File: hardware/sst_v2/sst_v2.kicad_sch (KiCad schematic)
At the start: 92 parts, among them U1 Pico_2_W, U2 ADS131M04IPWR, U3 DS3231SN, Y1 ECS-2520MVLC-081.92-BN-TR

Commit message: hw: Rev. 3 Review — LDO-Pinbelegung, VSYS-Diode, Verpolschutz, Fertigungsdaten
Fehler behoben:
- TPS7A4700: Symbol nach SBVS204G (GND-Pin lag an 3,3 V, OUT/IN vertauscht,
  ANY-OUT an 3,3 V), Footprint Texas RGW0020A, LDO-Bereich neu geroutet,
  Eingangs-C 10 uF (C22), Ausgangs-C 22 uF (C6)
- USB-VBUS speiste in den LiPo: Schottky D_VSYS1 zwischen +VBAT_SW und VSYS
- RTC-Backup-Diode verpolt: entfernt, CR1220 direkt an VBAT
- Buzzer-Footprint auf 5-mm-Raster (TDK PS1240P02BT)
- R18 an 3V3_EN entfernt, DS3231-RST offen
- ADS131M04 DVDD aus +3V3_DIG über FB1 (Logikpegel 3,3 V)
- CMC nach Murata-Ersatzschaltbild beschaltet (Gleichtaktdämpfung)
- J_DEBUG1 als 1x3 UART (SWD-Pins waren unverbunden)
- DRC: Lötstopp-Steg 0,1 mm, Kupfer-Kante 0,3 mm, J_SD1-Schirm-Pads gekürzt,
  volle Anbindung der GND-Pads

Empfehlungen umgesetzt: Verpolschutz Q_RP1 (DMG2305UX), Polymer-Tantal C26,
1 uF direkt an AVDD, 100 nF an 74HC4040 (C44), microSD-DAT1-Pull-up (R48),
Montagelöcher im Schaltplan, Silkscreen bereinigt.

ERC 0 Fehler, DRC 0 Fehler/0 offene Verbindungen/0 Paritätsfehler.
Gerber, Bohrdaten, BOM und CPL neu erzeugt. README für Rev. 3 neu.

Co-Authored-By: Claude Opus 5.5 <noreply@anthropic.com>
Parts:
- removed D_RTC1: 1N4148, Diode_SMD:D_SOD-123, symbol sst_v2_local:Diode
- removed R18: 10k, Resistor_SMD:R_0603_1608Metric, symbol sst_v2_local:R
- added C44: 100nF X7R, Capacitor_SMD:C_0603_1608Metric, symbol sst_v2_local:C
- added D_VSYS1: PMEG3020EH, Diode_SMD:D_SOD-123F, symbol sst_v2_local:Diode
- added H1, H2, H3, H4: M3_NPTH, MountingHole:MountingHole_3.2mm_M3, symbol sst_v2_local:MountingHole
- added Q_RP1: DMG2305UX, Package_TO_SOT_SMD:SOT-23, symbol sst_v2_local:DMG2305UX
- added R47: 10k, Resistor_SMD:R_0603_1608Metric, symbol sst_v2_local:R
- added R48: 47k, Resistor_SMD:R_0603_1608Metric, symbol sst_v2_local:R
- BZ1: footprint Buzzer_Beeper:Buzzer_12x9.5RM7.6 -> Buzzer_Beeper:Buzzer_TDK_PS1240P02BT_D12.2mm_H6.5mm
- C1: value 1uF X7R -> 100nF X7R
- C22: value 10uF X7R -> 10uF X5R; footprint Capacitor_SMD:C_0805_2012Metric -> Capacitor_SMD:C_0603_1608Metric
- C23: value 100nF X7R -> 1uF X7R
- C26: value 100uF/10V Tant -> 100uF 10V Polymer
- C6: value 10uF X7R -> 22uF X7R
- J_DEBUG1: value SWD+UART Header 1x5 -> UART Header 1x3; footprint Connector_PinHeader_2.54mm:PinHeader_1x05_P2.54mm_Vertical -> Connector_PinHeader_2.54mm:PinHeader_1x03_P2.54mm_Vertical; symbol sst_v2_local:Conn_5P -> sst_v2_local:Conn_1x03
- U_ANA_LDO1: footprint Package_DFN_QFN:QFN-20-1EP_5x5mm_P0.65mm_EP3.35x3.35mm -> Package_DFN_QFN:Texas_RGW0020A_VQFN-20-1EP_5x5mm_P0.65mm_EP3.15x3.15mm
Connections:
- net +3V0_ANA_FB is gone; now on net +3V3_DIG: U_ANA_LDO1.13 (EN), U_ANA_LDO1.15 (IN)
- net RTC_BAT_RAW is gone; now on net RTC_VBAT: BT1.1 (+)
- net SWCLK is gone; now on net GND: J_DEBUG1.3
- net +3V0_ANA: now also U_ANA_LDO1.1 (OUT), U_ANA_LDO1.20 (OUT), U_ANA_LDO1.3 (SENSE); no longer C22.1, FB1.1, U_ANA_LDO1.16 (OUT), U_ANA_LDO1.17 (OUT), U_ANA_LDO1.18 (OUT)
- net +3V3_DIG: now also C22.1, FB1.1, U_ANA_LDO1.16 (IN), C44.1, R48.2; no longer U3.4 (RST), U_ANA_LDO1.1 (IN), U_ANA_LDO1.12 (ANY7), U_ANA_LDO1.2 (IN), U_ANA_LDO1.3 (EN), U_ANA_LDO1.7 (ANY2), U_ANA_LDO1.8 (ANY3)
- net +VBAT: now also Q_RP1.2 (S); no longer J_BAT1.1
- net +VBAT_SW: now also D_VSYS1.2 (A); no longer U1.39 (VSYS)
- net FORK_POT_GND_F: now also L_FORK_CMC1.1; no longer L_FORK_CMC1.2
- net GND: now also U_ANA_LDO1.7 (GND), U_ANA_LDO1.8 (1P6V), C44.2, R47.2; no longer J_DEBUG1.5, U_ANA_LDO1.10 (ANY5), U_ANA_LDO1.11 (ANY6), U_ANA_LDO1.14 (GND), U_ANA_LDO1.5 (GND), U_ANA_LDO1.6 (ANY1), U_ANA_LDO1.9 (ANY4)
- net J_FORK_POT_GND: now also L_FORK_CMC1.2; no longer L_FORK_CMC1.1
- net J_SHOCK_POT_GND: now also L_SHOCK_CMC1.2; no longer L_SHOCK_CMC1.1
- net LDO_NRSS: now also U_ANA_LDO1.14 (NR); no longer U_ANA_LDO1.4 (NR/SS)
- net SHOCK_POT_GND_F: now also L_SHOCK_CMC1.1; no longer L_SHOCK_CMC1.2
- net +3V3_EN: no longer names the net of U1.37 (3V3_EN)
- net SD_NC2 renamed SD_DAT1
- net SD_DAT1: now also R48.1
- removed net SWDIO: J_DEBUG1.4
- new net Q_RP_G: Q_RP1.1 (G), R47.1
- new net VBAT_IN: J_BAT1.1, Q_RP1.3 (D)
- new net VSYS: D_VSYS1.1 (K), U1.39 (VSYS)
- no-connect marks 25 -> 31
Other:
- note added: "POWER — LiPo → SW → Schottky → VSYS +VBAT_SW → D_VSYS1 (PMEG3020EH) → VSYS (Pico) TPS7A4700: +3V3_DIG → +3V0_ANA"
- note added: "STORAGE / RTC / DISPLAY MicroSD J_SD on spi0 (GP16-19), VDD=+3V3_DIG DS3231 U3 on PIO-I2C (GP2/3), shared with OLED RTC_VBAT = CR1220 (BT1) direkt an U3 VBAT 4.7k pullups on DISP_SDA/SCL (mainboard, not OLED) OLED extern (J_OLED): SSD1306-Modul mit eigener Reg"
- note added: "UI — Buttons + Buzzer + Debug BTN_L/R: TL3315NF160Q, 10k pullup zu +3V3_DIG, 100nF debounce Buzzer: differential drive (BUZ_DRV_A → 47Ω → BZ pin1; BUZ_DRV_B → 47Ω → BZ pin2) BUZ_DRV_A/B sind GP22/GP21 PWM Slice A/B mit B_INV Debug: UART Header 1x3 (GP1 RX / GP0 TX / GND)"
- note added: "U_ANA_LDO — TPS7A4700 ultra-low-noise LDO +3V3_DIG → +3V0_ANA (4 µVrms) Vout = 1.4 V + 1.6 V: pin 8 (1P6V) an GND, andere ANY-OUT offen NR = 10 nF (C25), EN = +3V3_DIG, SENSE an OUT Input: C22 10 µF an +3V3_DIG; Output: C6 22 µF an +3V0_ANA"
- note removed: "POWER — LiPo → SW → VSYS +VBAT_SW feeds Pico VSYS; TPS7A4700-LDO from +3V3_DIG (Pico-onboard 3V3_OUT) → +3V0_ANA"
- note removed: "STORAGE / RTC / DISPLAY MicroSD J_SD on spi0 (GP16-19), VDD=+3V3_DIG DS3231 U3 on PIO-I2C (GP2/3), shared with OLED RTC_VBAT routed through 1N4148 from CR1220 (BT1) + 4.7µF glättung 4.7k pullups on DISP_SDA/SCL (mainboard, not OLED) OLED extern (J_OLED): SSD1306-Modul mit eigener Reg"
- note removed: "UI — Buttons + Buzzer + Debug BTN_L/R: TL3315NF160Q, 10k pullup zu +3V3_DIG, 100nF debounce Buzzer: differential drive (BUZ_DRV_A → 47Ω → BZ pin1; BUZ_DRV_B → 47Ω → BZ pin2) BUZ_DRV_A/B sind GP22/GP21 PWM Slice A/B mit B_INV Debug: 5-pin SWD (GND/SWDIO/SWCLK/UART_TX/UART_RX)"
- note removed: "U_ANA_LDO — TPS7A4700 ultra-low-noise LDO +3V3_DIG → +3V0_ANA (4 µVrms) Set pins ANY1-7 für 3.000 V: ANY2=ANY3=HIGH, rest LOW NR/SS = 10 nF (Soft-Start), EN = +3V3_DIG Input cap: 4.7 µF; Output stack: 10 µF + 100 nF + 10 nF"

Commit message: hw: Umplatzierung, Nacharbeit und Lader MCP73831
Umplatzierung:
- Pico 2 mm nach links, USB-Buchse innerhalb der Platine
- Poti-Eingang links, OLED/Taster rechts, Analogblock 2 mm nach rechts
- R49 (47k) an SD_DAT2, Y1-3D-Modell SG210

Nacharbeit:
- J_SD1 innerhalb der Kante und weg von H4
- BT1 und BZ1 getauscht, Einschubweg der Zelle frei
- C3 1,9 mm an U2 CAP, C40 2,7 mm an U_CLKBUF1 VCC
- Freiraum >= 3,5 mm um H3/H4

Lader:
- MCP73831 unter dem Pico, 300 mA, STAT-Teiler an GP6 (CHG_STAT)
- sst_v2.kicad_dru erlaubt Courtyard-Ueberdeckung mit U1 nur fuer die Lader-Teile

Digitalnetze neu geroutet (Freerouting, Sperrflaeche ueber Analogblock).
ERC 0 Fehler, DRC 0 Fehler / 0 offene Verbindungen.
Fertigungsdaten, BOM/CPL (102 Positionen) und README aktualisiert.

Co-Authored-By: Claude Opus 5.5 <noreply@anthropic.com>
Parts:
- added C_CHG1, C_CHG2: 4.7uF X5R, Capacitor_SMD:C_0805_2012Metric, symbol sst_v2_local:C
- added R49: 47k, Resistor_SMD:R_0603_1608Metric, symbol sst_v2_local:R
- added R_PROG: 3.3k 1%, Resistor_SMD:R_0603_1608Metric, symbol sst_v2_local:R
- added R_STAT1: 10k, Resistor_SMD:R_0603_1608Metric, symbol sst_v2_local:R
- added R_STAT2: 20k, Resistor_SMD:R_0603_1608Metric, symbol sst_v2_local:R
- added U_CHG1: MCP73831T-2ACI/OT, Package_TO_SOT_SMD:SOT-23-5, symbol sst_v2_local:MCP73831-2-OT
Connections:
- net +3V3_DIG: now also R49.2
- net +VBAT: now also C_CHG2.1, U_CHG1.3 (V_{BAT})
- net +VBUS: now also C_CHG1.1, U_CHG1.4 (V_{DD})
- net GND: now also C_CHG1.2, C_CHG2.2, R_PROG.2, R_STAT2.2, U_CHG1.2 (V_{SS})
- net SD_DAT2: now also R49.1
- net GP6_RSV renamed CHG_STAT
- net CHG_STAT: now also R_STAT1.2, R_STAT2.1
- new net CHG_PROG: R_PROG.1, U_CHG1.5 (PROG)
- new net CHG_STAT_5V: R_STAT1.1, U_CHG1.1 (STAT)
- no-connect marks 31 -> 30
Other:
- note added: "Lader Li-Po (USB über Pico-Buchse, VBUS = Pico Pin 40). I_CHG = 1000 V / R_PROG = 300 mA. CHG_STAT: Teiler 10k/20k, 5 V -> 3,3 V an GP6. Laden = 0 V, fertig = 3,3 V."

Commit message: hw: Schaltung — R_STAT2 15k, R50 in ADC_RST, +3V3_DVDD, Fiducials
- R_STAT2 20k -> 15k: CHG_STAT max. 3,15 V bei VBUS 5,25 V
- R50 100 Ohm zwischen GP7 (ADC_RST_MCU) und ADC_RST
- Netz +3V0_DVDD -> +3V3_DVDD, PWR_FLAG hinter FB1 (ERC-Warnung entfaellt)
- FID1-FID3 (Symbol Fiducial in sst_v2_local), Titelblock Rev. 3

Co-Authored-By: Claude Opus 5.5 <noreply@anthropic.com>
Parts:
- added FID1, FID2, FID3: Fiducial, Fiducial:Fiducial_1mm_Mask3mm, symbol sst_v2_local:Fiducial
- added R50: 100, Resistor_SMD:R_0603_1608Metric, symbol sst_v2_local:R
- R_STAT2: value 20k -> 15k
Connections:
- net ADC_RST: now also R50.2; no longer U1.10 (GP7)
- net +3V0_DVDD renamed +3V3_DVDD
- new net ADC_RST_MCU: R50.1, U1.10 (GP7)

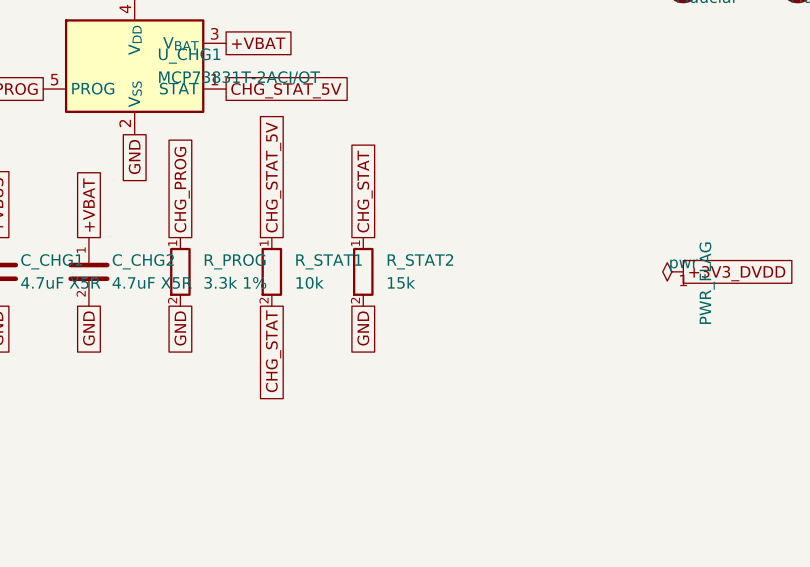
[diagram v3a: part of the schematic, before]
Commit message: hw: R_STAT2 10k (CHG_STAT max. 2,6 V), R50-Silkscreen 0,15 mm, Fertigungsdaten neu
Co-Authored-By: Claude Fable 5.1 <noreply@anthropic.com>
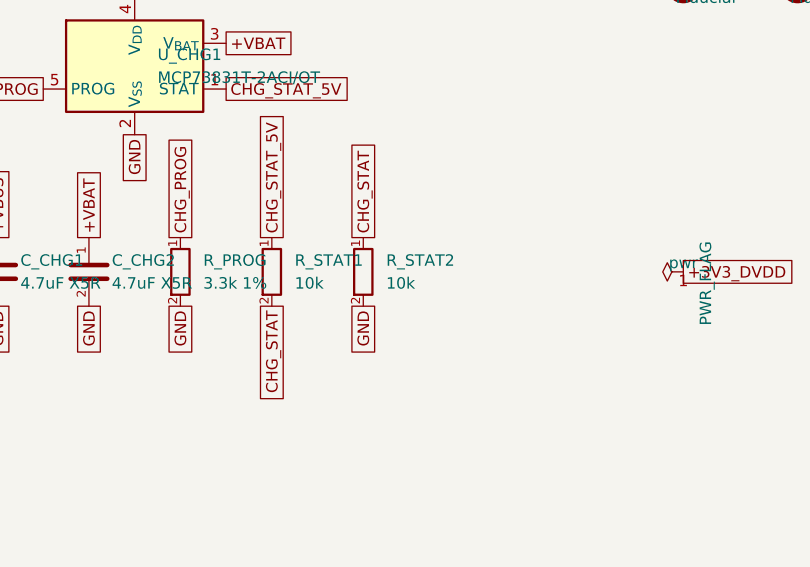
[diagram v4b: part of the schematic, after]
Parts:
- R_STAT2: value 15k -> 10k
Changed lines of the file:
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@@
 			)
 		)
-		(property "Value" "15k"
+		(property "Value" "10k"
 			(at 749.30 191.77 0)
 			(show_name no)

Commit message: hw: Testpads TP1-TP15, Soft-Power MAX16150, Fuel-Gauge MAX17048
Testpads: 15 SMD-Pads D 1,0 mm auf B.Cu (GND, Versorgungen, ADC-Takt,
Referenz, ADC-Eingaenge, IMU-Takt/-Versorgung), nicht bestueckt.

Soft-Power: J_PWR1 entfaellt. MAX16150A schaltet ueber Q_PWR1 (DMG2305UX)
+VBAT -> +VBAT_SW. SW_L ist Ein/Aus- und UI-Taster (PB_IN direkt, BTN_L
ueber RB751S40). GP28 = PWR_OFF (ueber 2N7002 an CLR), Teiler
VBAT_SENSE R19/R20/C29 entfaellt.

Fuel-Gauge: MAX17048 an +VBAT und I2C (0x36) fuer Ladestand und
Lade-Rate, auch bei ausgeschaltetem Geraet mit USB.

Ruhestrom aus: ca. 0,8 uA typ, 6,5 uA max. ERC 0 Fehler, DRC 0 Fehler,
0 offene Verbindungen, 0 Paritaetsfehler. Fertigungsdaten, BOM, CPL neu.

Co-Authored-By: Claude Opus 5.5 <noreply@anthropic.com>
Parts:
- removed C29: 100nF X7R, Capacitor_SMD:C_0603_1608Metric, symbol sst_v2_local:C
- removed J_PWR1: JST SH 2-pin (PWR switch), Connector_JST:JST_SH_BM02B-SRSS-TB_1x02-1MP_P1.00mm_Vertical, symbol sst_v2_local:Conn_2P1MP_SH
- removed R19, R20: 100k, Resistor_SMD:R_0603_1608Metric, symbol sst_v2_local:R
- added C_FG1, C_PWR1: 100nF X7R, Capacitor_SMD:C_0603_1608Metric, symbol sst_v2_local:C
- added D_PWR1: RB751S40, Diode_SMD:D_SOD-523, symbol sst_v2_local:Diode
- added Q_PWR1: DMG2305UX, Package_TO_SOT_SMD:SOT-23, symbol sst_v2_local:DMG2305UX
- added Q_PWR2, Q_PWR3: 2N7002, Package_TO_SOT_SMD:SOT-23, symbol sst_v2_local:2N7002
- added R_PWR1, R_PWR2, R_PWR3, R_PWR4: 100k, Resistor_SMD:R_0603_1608Metric, symbol sst_v2_local:R
- added TP1, TP15, TP2, TP3: GND, TestPoint:TestPoint_Pad_D1.0mm, symbol Connector:TestPoint
- added TP10: EXC, TestPoint:TestPoint_Pad_D1.0mm, symbol Connector:TestPoint
- added TP11: FORK, TestPoint:TestPoint_Pad_D1.0mm, symbol Connector:TestPoint
- added TP12: SHCK, TestPoint:TestPoint_Pad_D1.0mm, symbol Connector:TestPoint
- added TP13: 32K, TestPoint:TestPoint_Pad_D1.0mm, symbol Connector:TestPoint
- added TP14: IMU, TestPoint:TestPoint_Pad_D1.0mm, symbol Connector:TestPoint
- added TP4: 3V0A, TestPoint:TestPoint_Pad_D1.0mm, symbol Connector:TestPoint
- added TP5: DVDD, TestPoint:TestPoint_Pad_D1.0mm, symbol Connector:TestPoint
- added TP6: CLK, TestPoint:TestPoint_Pad_D1.0mm, symbol Connector:TestPoint
- added TP7: VBSW, TestPoint:TestPoint_Pad_D1.0mm, symbol Connector:TestPoint
- added TP8: VBAT, TestPoint:TestPoint_Pad_D1.0mm, symbol Connector:TestPoint
- added TP9: REF, TestPoint:TestPoint_Pad_D1.0mm, symbol Connector:TestPoint
- added U_FG1: MAX17048G+T10, Package_DFN_QFN:TDFN-8-1EP_2x2mm_P0.5mm_EP0.8x1.2mm, symbol sst_v2_local:MAX17048G+T10
- added U_PWR1: MAX16150AUT+T, Package_TO_SOT_SMD:SOT-23-6, symbol sst_v2_local:MAX16150AUT
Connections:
- net +3V0_ANA: now also TP4.1
- net +3V3_DVDD: now also TP5.1
- net +VBAT: now also C_FG1.1, C_PWR1.1, Q_PWR1.2 (S), R_PWR1.1, TP8.1, U_FG1.2 (CELL), U_FG1.3 (VDD), U_PWR1.3 (VCC)
- net +VBAT_SW: now also Q_PWR1.3 (D), TP7.1
- net ADC_CLKIN: now also TP6.1
- net BTN_L: now also D_PWR1.2 (A); no longer SW_L1.2
- net DISP_SCL: now also U_FG1.7 (SCL)
- net DISP_SDA: now also U_FG1.8 (SDA)
- net EXC_REF: now also TP9.1
- net FORK_AIN_P: now also TP11.1
- net GND: now also C_FG1.2, C_PWR1.2, Q_PWR2.2 (S), Q_PWR3.2 (S), R_PWR2.2, R_PWR4.2, TP1.1, TP15.1, TP2.1, TP3.1, U_FG1.1 (CTG), U_FG1.4 (GND), U_FG1.6 (QSTRT), U_FG1.9 (EP), U_PWR1.2 (GND)
- net IMU_3V3: now also TP14.1
- net IMU_CLK32K: now also TP13.1
- net POT_EXC: now also TP10.1
- net SHOCK_AIN_P: now also TP12.1
- net VBAT_SENSE renamed PWR_OFF
- net PWR_OFF: now also Q_PWR3.1 (G), R_PWR4.1
- new net PSW_EN: Q_PWR2.1 (G), R_PWR2.1, R_PWR3.1, U_PWR1.4 (OUT)
- new net PSW_GATE: Q_PWR1.1 (G), Q_PWR2.3 (D), R_PWR1.2
- new net PWR_BTN: D_PWR1.1 (K), SW_L1.2, U_PWR1.1 (PB_IN)
- new net PWR_CLR: Q_PWR3.3 (D), R_PWR3.2, U_PWR1.6 (~{CLR})
- no-connect marks 30 -> 31
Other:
- note added: "POWER — LiPo → Q_RP1 → Q_PWR1 (Soft-Power MAX16150) → Schottky → VSYS +VBAT_SW → D_VSYS1 (PMEG3020EH) → VSYS (Pico) TPS7A4700: +3V3_DIG → +3V0_ANA"
- note added: "Soft-Power + Fuel-Gauge (Rev. 3, 2026-10-03) SW_L1 (Taster links) -> PWR_BTN -> U_PWR1 PB_IN (interner Pull-up 1,4 MOhm an VCC). BTN_L (GP4, R27 10k an +3V3_DIG) ueber D_PWR1 RB751S40 an PWR_BTN: Taste bleibt UI-Taste. U_PWR1 OUT -> PSW_EN -> Q_PWR2 -> PSW_GATE low -> Q_PWR1 (P-MOS) leitet: +VBAT -> +VBAT_SW. Aus: GP28 PWR_OFF high -> Q_PWR3 zieht CLR low -> OUT low. Taste > 8 s halten = Hardware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"
- note added: "Testpads (Unterseite, nicht bestückt) TP1..TP15: SMD-Pad D1,0 mm auf B.Cu, nicht in BOM/CPL"
- note removed: "POWER — LiPo → SW → Schottky → VSYS +VBAT_SW → D_VSYS1 (PMEG3020EH) → VSYS (Pico) TPS7A4700: +3V3_DIG → +3V0_ANA"
